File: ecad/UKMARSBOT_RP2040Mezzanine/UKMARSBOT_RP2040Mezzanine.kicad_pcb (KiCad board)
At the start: 2 copper layers, 62.5 x 81.3 mm, 16 parts, among them J1 Conn_01x16, J2 Conn_01x06, J3 Conn_01x06, J4 Conn_01x06, J5 Conn_01x06, SW1 TACT_SW, SW2 TACT_SW, U1 Pico

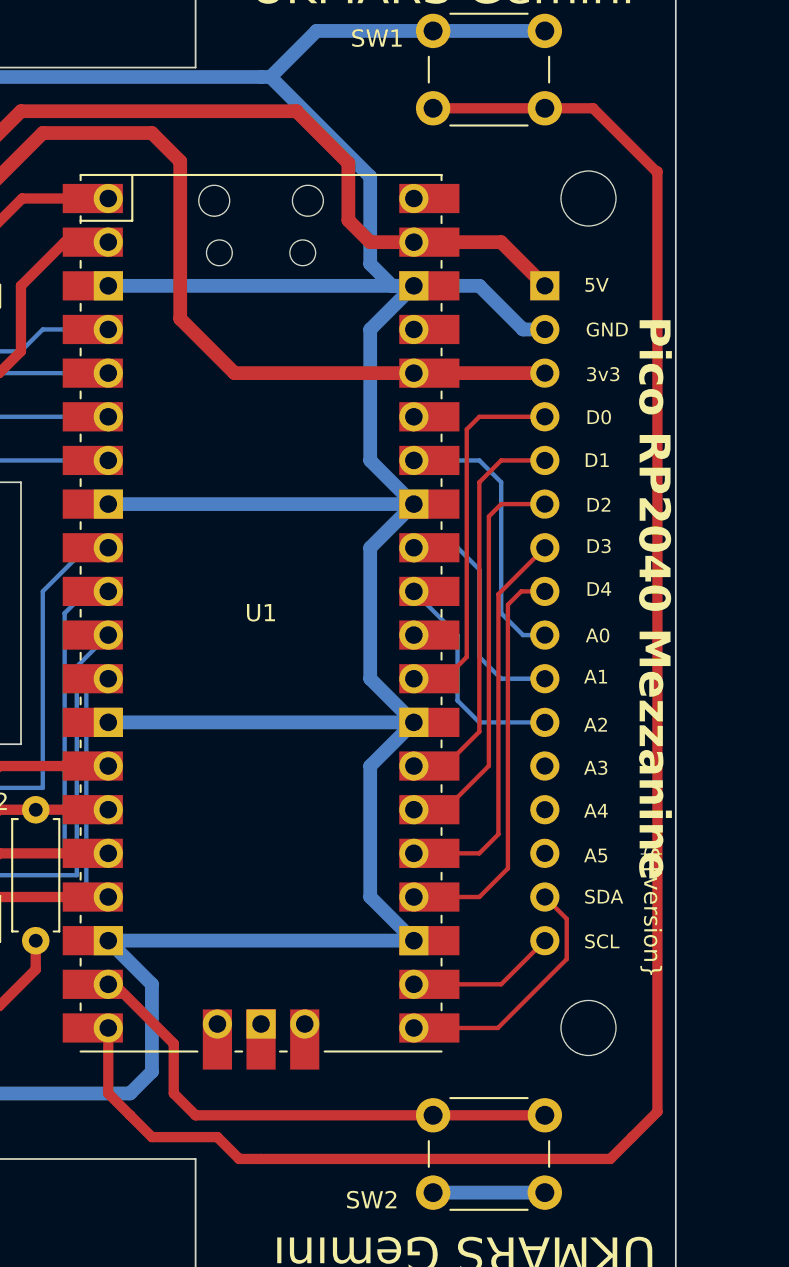
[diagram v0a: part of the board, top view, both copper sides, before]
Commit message: Revised lime sensor board and sensor mounting hole moved forward 1.27mm for connector
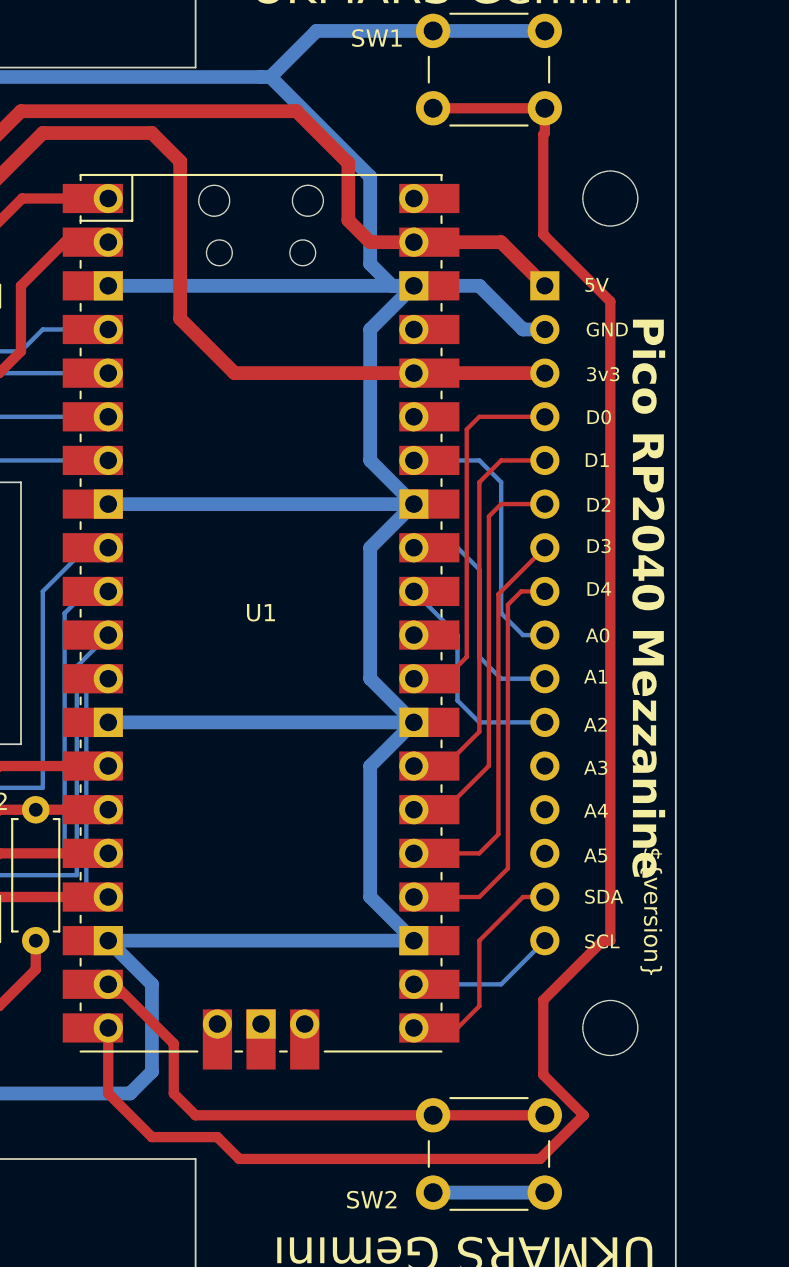
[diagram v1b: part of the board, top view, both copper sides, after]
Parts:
- moved H3 1.27 mm to (161.3, 77.5)
- moved H4 1.27 mm to (161.3, 125.7)
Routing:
- net GPIO15: track 107.8 -> 103.7 mm
- net SDA: track 14.7 -> 13.0 mm
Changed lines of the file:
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@@
 	(footprint "ukmarsbot:MountingHole_3.2mm_M3_clearance"
 		(layer "F.Cu")
-		(at 160.02 125.73)
+		(at 161.29 125.73)
 		(descr "Mounting Hole 3.2mm, no annular, M3")
 		(tags "mounting hole 3.2mm no annular m3")
@@
 	(footprint "ukmarsbot:MountingHole_3.2mm_M3_clearance"
 		(layer "F.Cu")
-		(at 160.02 77.47)
+		(at 161.29 77.47)
 		(descr "Mounting Hole 3.2mm, no annular, M3")
 		(tags "mounting hole 3.2mm no annular m3")
@@
 	)
 	(gr_text "Pico RP2040 Mezzanine"
-		(at 163.83 100.74 270)
+		(at 163.437895 100.702569 270)
 		(layer "F.SilkS")
 		(effects
@@
 	)
 	(segment
-		(start 160.285433 72.22)
-		(end 163.961627 75.896194)
+		(start 161.29 120.65)
+		(end 161.29 83.46)
 		(width 0.6)
 		(layer "F.Cu")
@@
 	)
 	(segment
-		(start 164.03102 75.896194)
-		(end 164.03102 130.60898)
+		(start 132.08 129.54)
+		(end 134.62 132.08)
 		(width 0.6)
 		(layer "F.Cu")
@@
 	)
 	(segment
-		(start 161.29 133.35)
-		(end 162.56 132.08)
+		(start 157.48 73.66)
+		(end 157.39 73.75)
 		(width 0.6)
 		(layer "F.Cu")
@@
 	)
 	(segment
-		(start 138.43 132.08)
-		(end 139.7 133.35)
+		(start 157.39 128.457258)
+		(end 157.39 124.114567)
 		(width 0.6)
 		(layer "F.Cu")
@@
 	)
 	(segment
-		(start 139.7 133.35)
-		(end 140.97 133.35)
+		(start 157.48 72.22)
+		(end 150.98 72.22)
 		(width 0.6)
 		(layer "F.Cu")
@@
 	)
 	(segment
-		(start 157.48 72.22)
-		(end 150.98 72.22)
+		(start 161.29 83.46)
+		(end 157.48 79.65)
 		(width 0.6)
 		(layer "F.Cu")
@@
 	)
 	(segment
-		(start 133.35 130.81)
-		(end 134.62 132.08)
+		(start 157.39 79.56)
+		(end 157.48 79.65)
 		(width 0.6)
 		(layer "F.Cu")
@@
 	)
 	(segment
-		(start 132.08 129.54)
-		(end 133.35 130.81)
+		(start 138.43 132.08)
+		(end 139.7 133.35)
 		(width 0.6)
 		(layer "F.Cu")
@@
 	)
 	(segment
-		(start 132.08 125.73)
-		(end 132.08 129.54)
+		(start 159.742742 130.81)
+		(end 157.39 128.457258)
+		(width 0.6)
+		(layer "F.Cu")
+		(net 16)
+	)
+	(segment
+		(start 157.48 72.22)
+		(end 157.48 73.66)
+		(width 0.6)
+		(layer "F.Cu")
+		(net 16)
+	)
+	(segment
+		(start 160.854567 120.65)
+		(end 161.29 120.65)
 		(width 0.6)
 		(layer "F.Cu")
@@
 	)
 	(segment
-		(start 163.961627 75.896194)
-		(end 164.03102 75.896194)
+		(start 157.39 73.75)
+		(end 157.39 79.56)
 		(width 0.6)
 		(layer "F.Cu")
@@
 	)
 	(segment
-		(start 140.97 133.35)
-		(end 161.29 133.35)
+		(start 132.08 125.73)
+		(end 132.08 129.54)
 		(width 0.6)
 		(layer "F.Cu")
@@
 	)
 	(segment
-		(start 157.48 72.22)
-		(end 160.285433 72.22)
+		(start 157.202742 133.35)
+		(end 159.742742 130.81)
 		(width 0.6)
 		(layer "F.Cu")
@@
 	)
 	(segment
-		(start 162.56 132.08)
-		(end 164.03102 130.60898)
+		(start 157.39 124.114567)
+		(end 160.854567 120.65)
+		(width 0.6)
+		(layer "F.Cu")
+		(net 16)
+	)
+	(segment
+		(start 139.7 133.35)
+		(end 157.202742 133.35)
 		(width 0.6)
 		(layer "F.Cu")
@@
 	)
 	(segment
-		(start 149.86 125.73)
-		(end 154.749226 125.73)
+		(start 156.21 118.11)
+		(end 157.48 118.11)
 		(width 0.254)
 		(layer "F.Cu")
@@
 	)
 	(segment
-		(start 158.757 119.387)
-		(end 157.48 118.11)
+		(start 152.4 125.73)
+		(end 153.67 124.46)
 		(width 0.254)
 		(layer "F.Cu")
@@
 	)
 	(segment
-		(start 158.757 121.722226)
-		(end 158.757 119.387)
+		(start 153.67 124.46)
+		(end 153.67 120.65)
 		(width 0.254)
 		(layer "F.Cu")
@@
 	)
 	(segment
-		(start 154.749226 125.73)
-		(end 158.757 121.722226)
+		(start 153.67 120.65)
+		(end 156.21 118.11)
 		(width 0.254)
 		(layer "F.Cu")
@@
 	)
 	(segment
-		(start 154.94 123.19)
-		(end 157.48 120.65)
+		(start 149.86 125.73)
+		(end 152.4 125.73)
 		(width 0.254)
 		(layer "F.Cu")
-		(net 20)
+		(net 19)
 	)
 	(segment
@@
 		(end 154.94 123.19)
 		(width 0.254)
-		(layer "F.Cu")
+		(layer "B.Cu")
+		(net 20)
+	)
+	(segment
+		(start 154.94 123.19)
+		(end 157.48 120.65)
+		(width 0.254)
+		(layer "B.Cu")
 		(net 20)
 	)

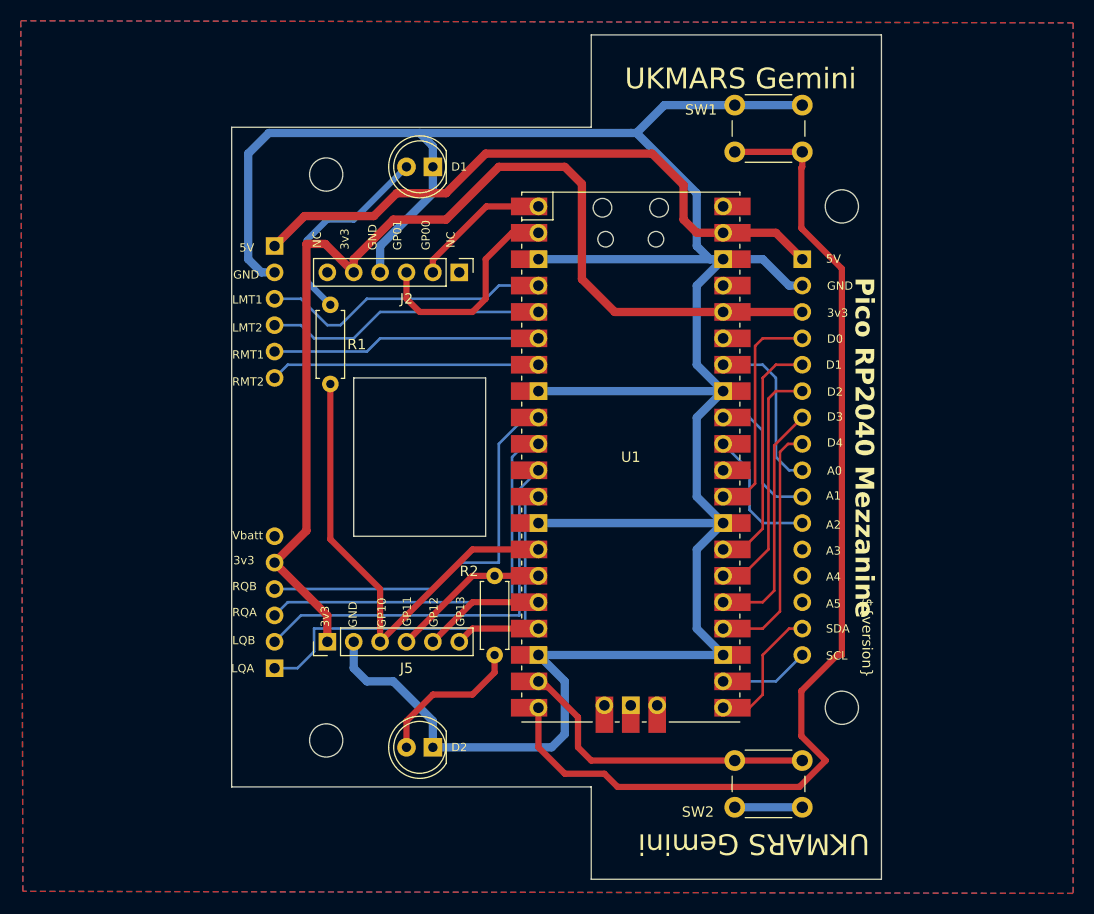
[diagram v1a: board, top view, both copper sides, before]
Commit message: Revised Wall Sensor Board consistent with hole and connector position. Fabrication files created.
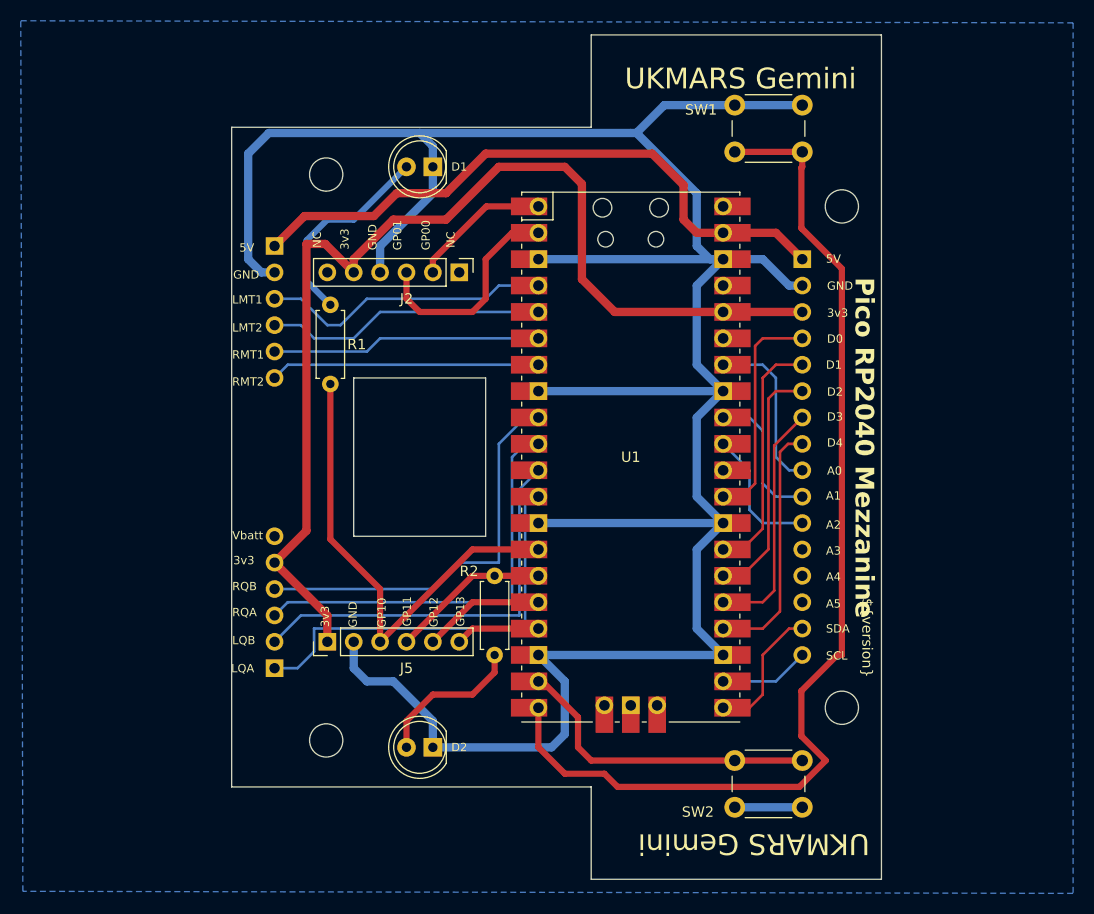
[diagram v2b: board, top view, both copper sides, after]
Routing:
- removed copper zone on F.Cu, net GND
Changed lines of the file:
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@@
 			(outputformat 1)
 			(mirror no)
-			(drillshape 1)
+			(drillshape 0)
 			(scaleselection 1)
-			(outputdirectory "")
+			(outputdirectory "fab/")
 		)
 	)
@@
 		(net 1)
 		(net_name "GND")
-		(layers "F&B.Cu")
+		(layer "B.Cu")
 		(hatch edge 0.508)
 		(connect_pads

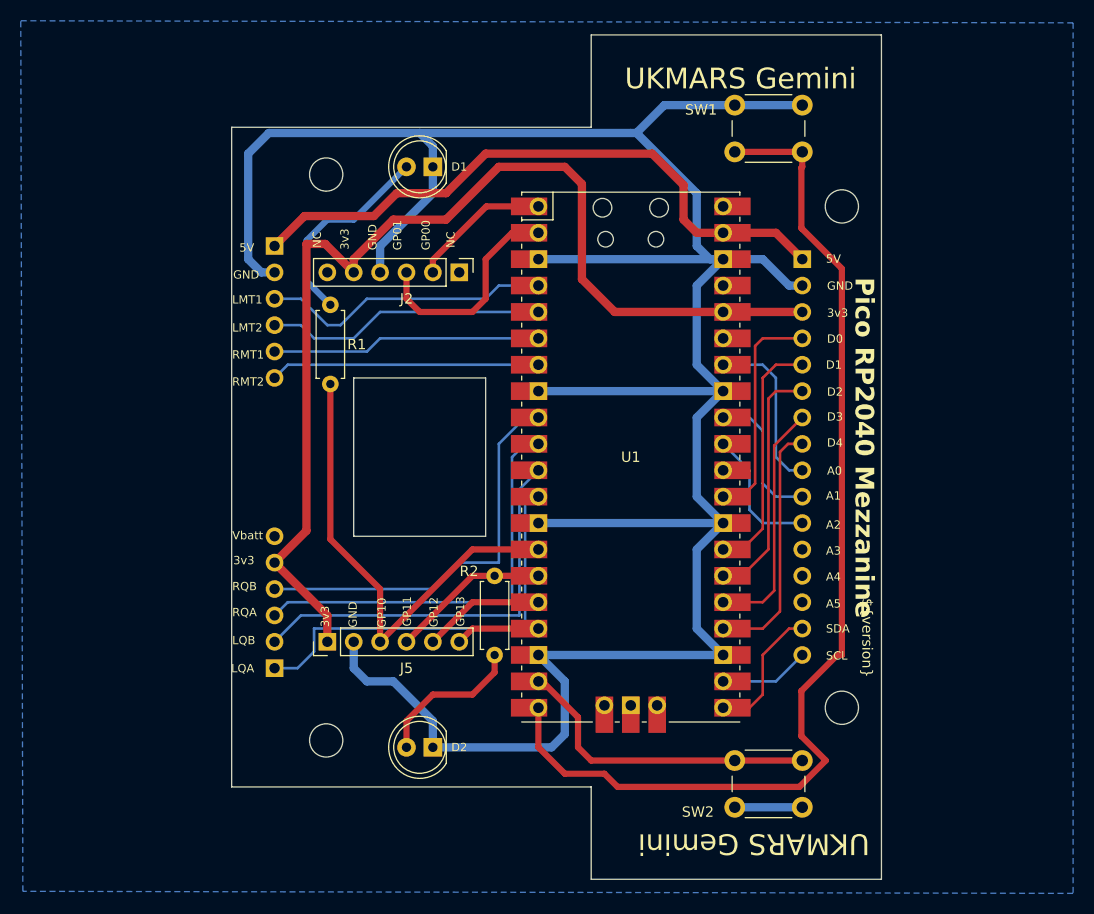
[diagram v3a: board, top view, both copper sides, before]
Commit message: Updated Mezzanine for PiPico
Updated for v2.0 board set addressing all issues raised on the prototype board.
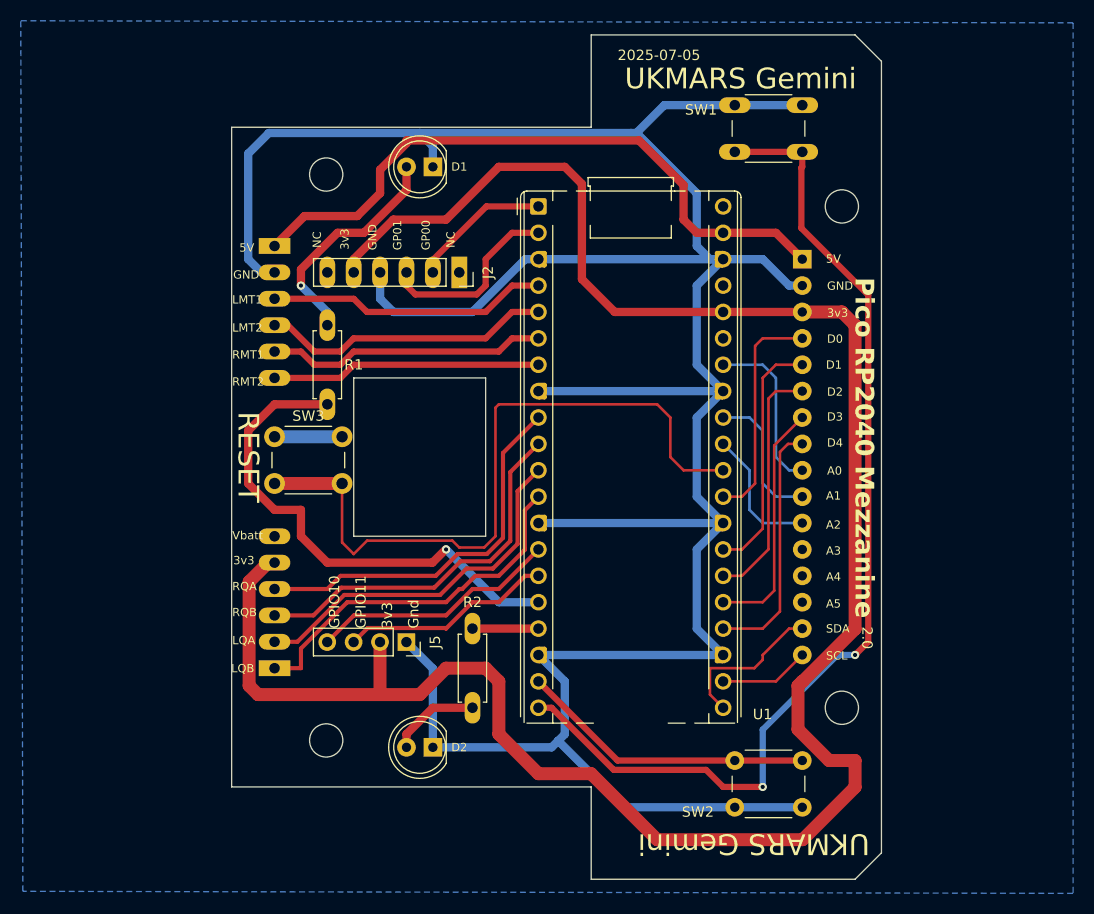
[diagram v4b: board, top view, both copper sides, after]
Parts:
- added SW3: TACT_SW, Button_Switch_THT:SW_PUSH_6mm, F.Cu at (106.7, 99.6)
- J2: footprint Connector_PinHeader_2.54mm:PinHeader_1x06_P2.54mm_Vertical -> Connector_PinSocket_2.54mm:PinSocket_1x06_P2.54mm_Vertical
- J5: value Conn_01x06 -> Conn_01x04_Pin; footprint Connector_PinHeader_2.54mm:PinHeader_1x06_P2.54mm_Vertical -> Connector_PinSocket_2.54mm:PinSocket_1x04_P2.54mm_Vertical
- U1: footprint MCU_RaspberryPi_and_Boards:RPi_Pico_SMD_TH -> Module:RaspberryPi_Pico_Common_THT
- moved U1 25.7 mm to (132.1, 77.5)
- moved J5 7.61 mm to (119.4, 119.4), turned to -90 degrees
- moved R2 5.50 mm to (125.7, 118.1)
- moved R1 1.98 mm to (111.8, 96.5)
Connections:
- J4 pad 1: LQA -> LQB
- J4 pad 2: LQB -> LQA
- J4 pad 3: RQA -> RQB
- J4 pad 4: RQB -> RQA
- J5 pad 1: 3v3 -> GND
- J5 pad 2: GND -> 3v3
- J5 pad 3: GPIO10 -> GPIO11
- J5 pad 4: GPIO11 -> GPIO10
- R1 pad 1: GPIO10 -> GPIO12
- R2 pad 1: GPIO11 -> GPIO13
- U1 pad 10: RQA -> RQB
- U1 pad 11: LQB -> LQA
- U1 pad 12: LQA -> LQB
- U1 pad 30: unconnected-(U1-RUN-Pad30) -> RUN
- U1 pad 9: RQB -> RQA
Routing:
- net 3v3: track 106.6 -> 205.3 mm
- net RUN: track 0.00 -> 67.9 mm
- net GPIO12: track 11.7 -> 49.0 mm, vias 0 -> 1
- net GND: track 268.3 -> 299.0 mm
- net GPIO10: track 45.7 -> 24.0 mm
- net Net-(D2-A): track 14.6 -> 8.67 mm
- net LQA: track 41.0 -> 35.2 mm
- net GPIO11: track 15.3 -> 20.5 mm
- net GPIO15: track 103.7 -> 100.3 mm, vias 0 -> 2
- net RQA: track 40.4 -> 37.0 mm
- net GPIO01: track 21.2 -> 18.3 mm
- net RQB: track 38.9 -> 36.1 mm
- net LQB: track 39.3 -> 36.6 mm
- net 5V: track 60.6 -> 63.2 mm
- net Net-(D1-A): track 19.7 -> 22.0 mm, vias 0 -> 1
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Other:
- outline, holes or cut-outs redrawn
- board text added: "101.6"
- board text added: "2.0"
- board text added: "2025-07-05"
- board text added: "GPIO10"
- board text added: "GPIO11"
- board text added: "Gnd"
- board text added: "RESET"
- board text removed: "${version}"
- board text removed: "GP10"
- board text removed: "GP11"
- board text removed: "GP12"
- board text removed: "GP13"
